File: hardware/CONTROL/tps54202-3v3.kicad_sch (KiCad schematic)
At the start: 12 parts, among them U3 TPS54202DDC

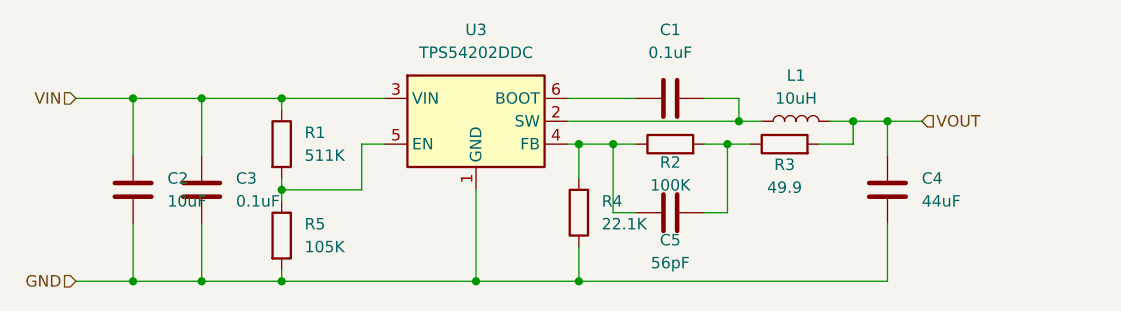
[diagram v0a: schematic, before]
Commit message: PD24 控制部分的PCB设计完成
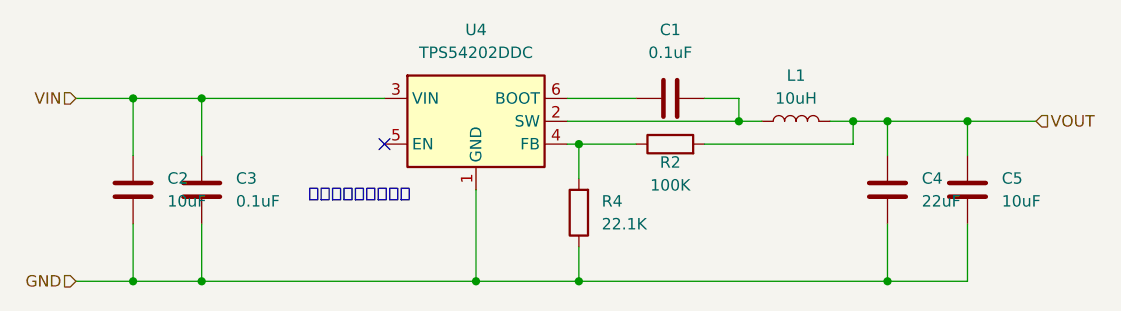
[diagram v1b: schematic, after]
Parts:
- removed R1: 511K, symbol Device:R
- removed R3: 49.9, symbol Device:R
- removed R5: 105K, symbol Device:R
- C1, C2, C3: footprint (none) -> Capacitor_SMD:C_0603_1608Metric
- C4: value 44uF -> 22uF; footprint (none) -> Capacitor_SMD:C_0603_1608Metric
- C5: value 56pF -> 10uF; footprint (none) -> Capacitor_SMD:C_0603_1608Metric
- L1: footprint (none) -> Inductor_SMD:L_Abracon_ASPI-3012S
- R2, R4: footprint (none) -> Resistor_SMD:R_0603_1608Metric
- renumbered U3 to U4
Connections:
- net GND: now also C5.2
- net VOUT: now also C5.1, R2.2
- net at R2.1, R4.2, U4.4 (FB): no longer C5.1
- no-connect marks 0 -> 1
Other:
- note added: "使能脚悬空即可启用"
